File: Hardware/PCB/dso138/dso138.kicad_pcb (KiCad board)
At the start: 2 copper layers, 94 x 85 mm, 41 parts, among them J1 Synth_power_2x5, J2 Conn_01x02, J3 Conn_01x02, J4 Conn_01x02, J5 Conn_02x04_Odd_Even, J6 Conn_02x04_Odd_Even, J7 Conn_02x04_Odd_Even, J8 Conn_02x04_Odd_Even, J9 Conn_01x02, SW1 SW_Push, SW2 SW_Push, SW3 SW_Push, SW4 SW_Push, SW5 SW_Push, SW6 SW_DP3T, SW7 SW_DP3T, SW8 SW_DP3T, U1 TL072, U2 L78L09_TO92

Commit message: KiCad 7; Reorg schematic and add panel components & connectors; re-enable 3D models
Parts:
- C1, C2, C5: footprint ao_tht:CP_Radial_D6.3mm_P2.50mm -> AO_tht:CP_Radial_D6.3mm_P2.50mm
- C3, C4, C6: footprint ao_tht:C_Disc_D3.0mm_W1.6mm_P2.50mm -> AO_tht:C_Disc_D3.0mm_W1.6mm_P2.50mm
- D1, D2: footprint ao_tht:D_DO-41_SOD81_P10.16mm_Horizontal -> AO_tht:D_DO-41_SOD81_P10.16mm_Horizontal
- D3: footprint ao_tht:LED_D5.0mm -> AO_tht:LED_D5.0mm
- GRAF2: footprint ao_tht:CC0_logo -> AO_tht:CC0_logo
- GRAF3: footprint ao_tht:analogoutput -> AO_tht:analogoutput
- H1, H2, H3, H4: footprint ao_tht:MountingHole_3.2mm_Pad -> AO_tht:MountingHole_3.2mm_Pad
- J1: footprint ao_tht:Power_Header -> AO_tht:Power_Header
- R1, R2: footprint ao_tht:R_Axial_DIN0207_L6.3mm_D2.5mm_P10.16mm_Horizontal -> AO_tht:R_Axial_DIN0207_L6.3mm_D2.5mm_P10.16mm_Horizontal
- SW1, SW2, SW3, SW4, SW5: footprint ao_tht:Tactile_E-switch_TL1100F160Q -> AO_tht:Tactile_E-switch_TL1100F160Q
- TP1, TP2, TP3, TP4: footprint ao_tht:TestPoint_THTPad_D1.5mm_Drill0.7mm -> AO_tht:TestPoint_THTPad_D1.5mm_Drill0.7mm
- U1: footprint ao_tht:DIP-8_W7.62mm_Socket_LongPads -> AO_tht:DIP-8_W7.62mm_Socket_LongPads
- U2: footprint ao_tht:TO-92_Inline_Wide -> AO_tht:TO-92_Inline_Wide
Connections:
- net /+12_IN renamed /Controls board/+12_IN
- net /-12_IN renamed /Controls board/-12_IN

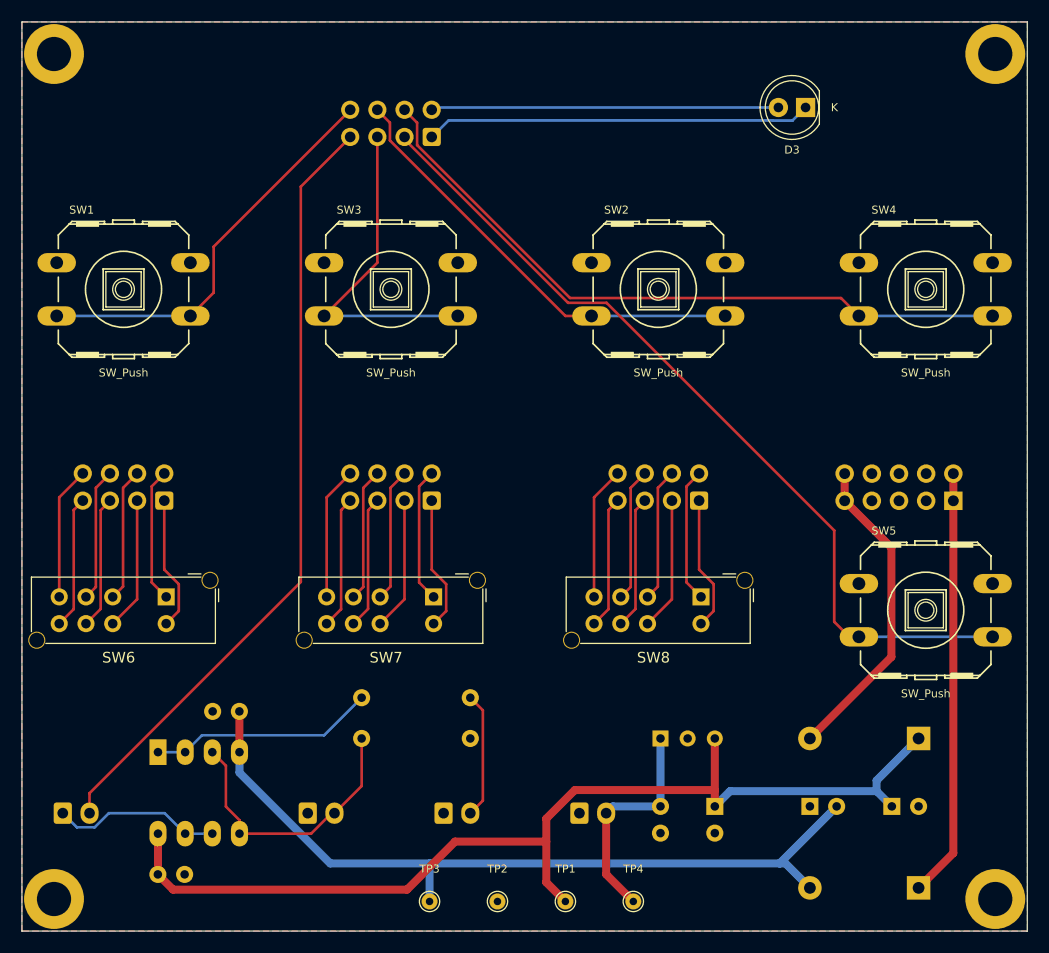
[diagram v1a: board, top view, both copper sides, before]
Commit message: TO-220 regulator; panel
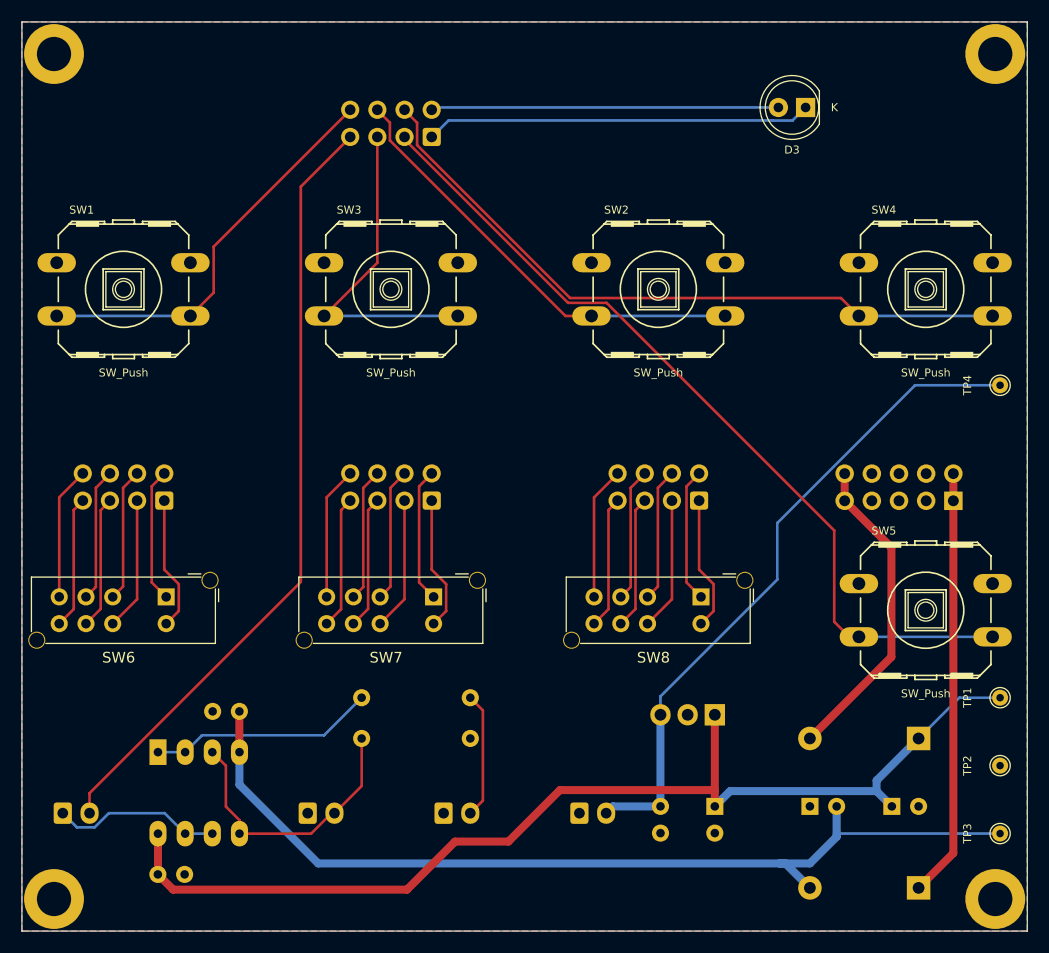
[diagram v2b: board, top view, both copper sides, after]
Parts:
- removed U2: L78L09_TO92, AO_tht:TO-92_Inline_Wide
- added U3: LM7809_TO220, Package_TO_SOT_THT:TO-220-3_Vertical, B.Cu at (117.8, 144.8)
- moved TP4 59.2 mm to (144.4, 114.0), turned to 90 degrees
- moved TP3 53.7 mm to (144.4, 155.9), turned to 90 degrees
- moved TP2 48.7 mm to (144.4, 149.5), turned to 90 degrees
- moved TP1 44.9 mm to (144.4, 143.2), turned to 90 degrees
- moved GRAF3 2.84 mm to (68.2, 91.1)
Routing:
- net +9V: track 21.0 -> 62.5 mm
- net -12V: track 74.6 -> 88.7 mm
- net +12V: track 98.5 -> 102.4 mm
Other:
- board text added: "DSO138 module Rich Holmes 2/2023 CC0 1.0 https://github.com/holmesrichards/dso138"
- board text removed: "DSO138 module Rich Holmes 11/2022 CC0 1.0 https://github.com/holmesrichards/dso138"

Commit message: Net classes, move 7809 and make horizontal, inverting buffers, power switch via PCB
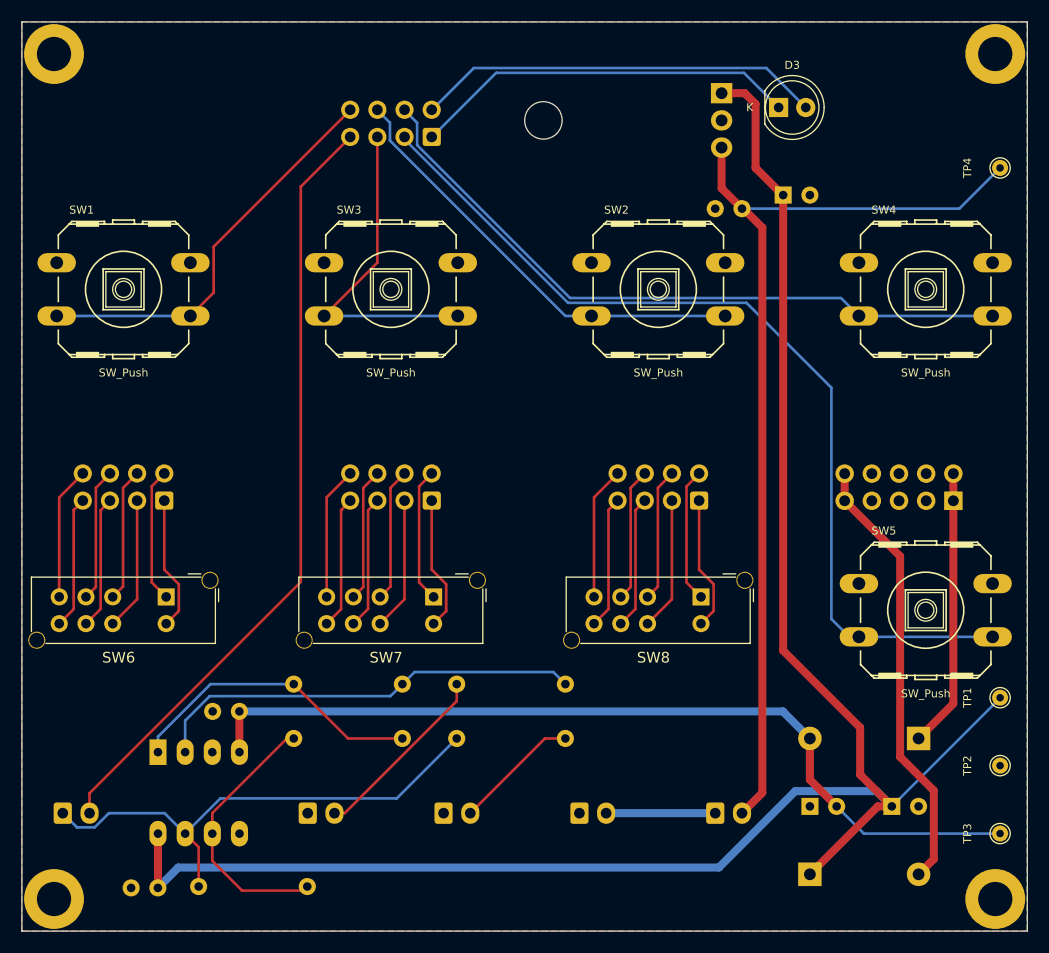
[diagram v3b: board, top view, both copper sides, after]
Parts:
- added J21: Conn_01x02, Connector_JST:JST_XH_B2B-XH-A_1x02_P2.50mm_Vertical, B.Cu at (117.8, 154.0)
- added R3: 100k, AO_tht:R_Axial_DIN0207_L6.3mm_D2.5mm_P10.16mm_Horizontal, B.Cu at (88.6, 141.9)
- added R4: 10k, AO_tht:R_Axial_DIN0207_L6.3mm_D2.5mm_P10.16mm_Horizontal, B.Cu at (88.6, 147.0)
- added R5: 10k, AO_tht:R_Axial_DIN0207_L6.3mm_D2.5mm_P10.16mm_Horizontal, B.Cu at (79.7, 160.8)
- R1: value 1M -> 100k
- U3: footprint Package_TO_SOT_THT:TO-220-3_Vertical -> Package_TO_SOT_THT:TO-220-3_Horizontal_TabDown
- moved U3 58.1 mm to (118.4, 86.7), turned to -90 degrees
- moved C5 57.5 mm to (124.2, 96.2), turned to 0 degrees
- moved C6 56.4 mm to (120.3, 97.5), turned to 180 degrees
- moved GRAF2 30.3 mm to (87.3, 111.4)
- moved TP4 20.3 mm to (144.4, 93.7)
- moved D1 16.3 mm to (126.7, 159.7), turned to 0 degrees
- moved D2 14.0 mm to (136.8, 147.0)
- moved R1 10.2 mm to (93.7, 141.9)
- moved R2 9.67 mm to (93.7, 147.0)
- moved D3 2.52 mm to (123.7, 88.0), turned to 0 degrees
- moved C3 1.26 mm to (65.7, 161.0), turned to 180 degrees
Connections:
- J9 pad 2: +9V -> /9V_SWITCHED
- R1 pad 2: GND -> Net-(U1A--)
- R2 pad 1: Net-(U1A--) -> /AUDIO_BUF
- U1 pad 1: Net-(U1A--) -> Net-(R3-Pad2)
- U1 pad 3: /AUDIO_IN -> GND
- U1 pad 5: /AUDIO_IN -> GND
- U1 pad 6: /AUDIO_BUF -> Net-(U1B--)
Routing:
- net +12V: track 102.4 -> 177.2 mm
- net /AUDIO_BUF: track 15.9 -> 47.9 mm
- net Net-(R3-Pad2): track 0.00 -> 28.4 mm
- net +9V: track 62.5 -> 90.3 mm
- net Net-(U1B--): track 0.00 -> 25.2 mm
- net Net-(U1A--): track 21.1 -> 40.8 mm
- net /Controls board/-12_IN: track 40.1 -> 26.1 mm
- net /Controls board/+12_IN: track 29.7 -> 41.5 mm
- net /9V_SWITCHED: track 0.00 -> 10.2 mm
- net /AUDIO_IN: track 26.1 -> 17.4 mm
- net /SW_RESET: track 78.3 -> 86.0 mm
- net -12V: track 88.7 -> 81.9 mm
- net /LED_A: track 32.2 -> 37.8 mm
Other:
- board text added: "PWR SWITCH"

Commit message: Mechanicals
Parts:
- renumbered GRAF2 to GRAF1, GRAF3 to GRAF2, J5 to J10, J6 to J11, J7 to J12, J8 to J13, J9 to J14, J1 to J20, J2 to J6, J3 to J7, J4 to J8, J21 to J9, R3 to R2, R4 to R3, R5 to R4, R2 to R5, SW6 to SW1, SW7 to SW2, SW8 to SW3, SW1 to SW4, SW2 to SW5, SW3 to SW6, SW4 to SW7, SW5 to SW8, U3 to U2
